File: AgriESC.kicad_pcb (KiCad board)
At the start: 2 copper layers, 94.5 x 53.5 mm, 309 parts, among them J1 SUPPLY, J10 GPIO, J11 USB_OTG, J12 HALL_ENC, J2 PH_A, J3 PH_B, J4 PH_C, J6 COMM, J7 SERVO, J8 CAN, J9 SWD, SW1 SW_SPDT, U1 FDMS7698, U10 STM32F405RGT6, U11 DRV8303, U12 TJA1051TK-3, U13 LMR16006YQ, U14 MCP1700-3302E_SOT23, U15 MCP1700-3302E_SOT23, U2 FDMS7698, U3 FDMS7698, U4 FDMS7698, U5 FDMS7698, U6 FDMS7698, U7 MAX9920, U8 MAX9920, U9 MAX9920, Y1 8M Resonator

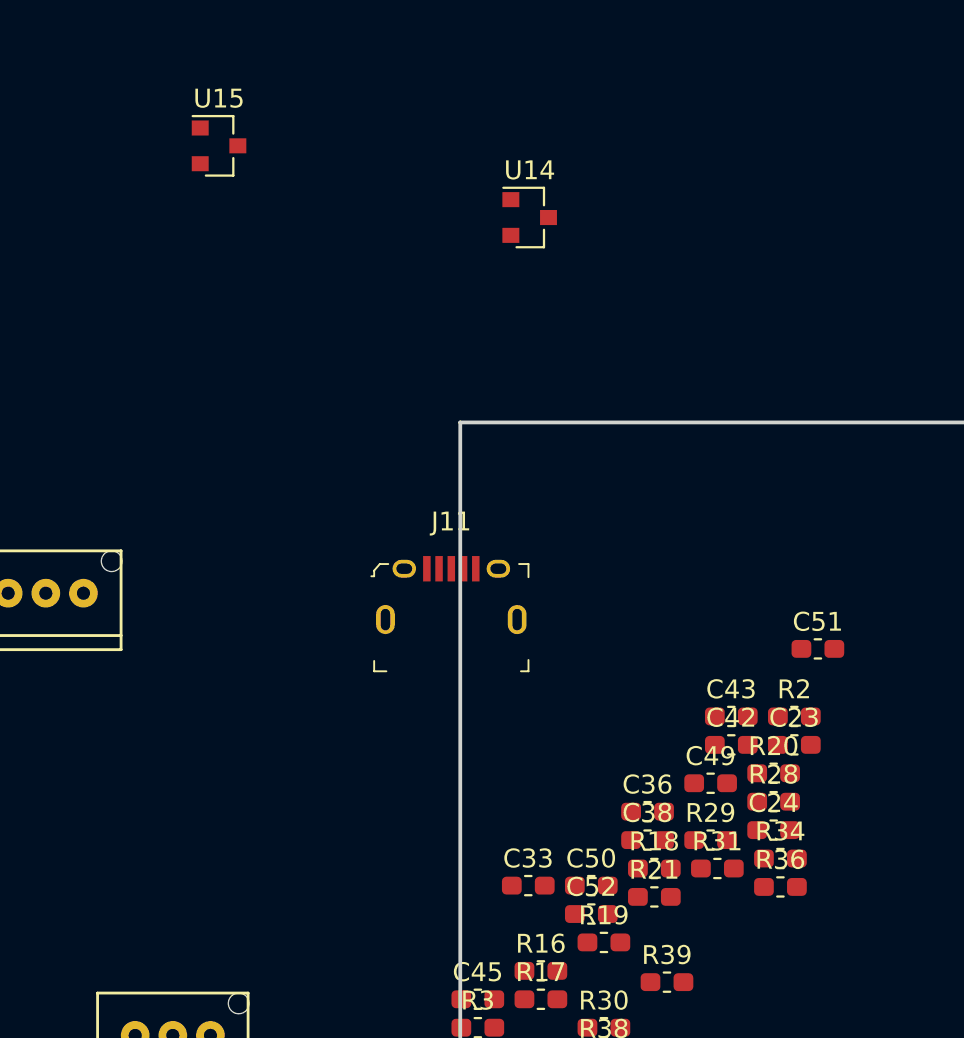
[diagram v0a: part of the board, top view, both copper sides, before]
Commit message: Wired up LDOs
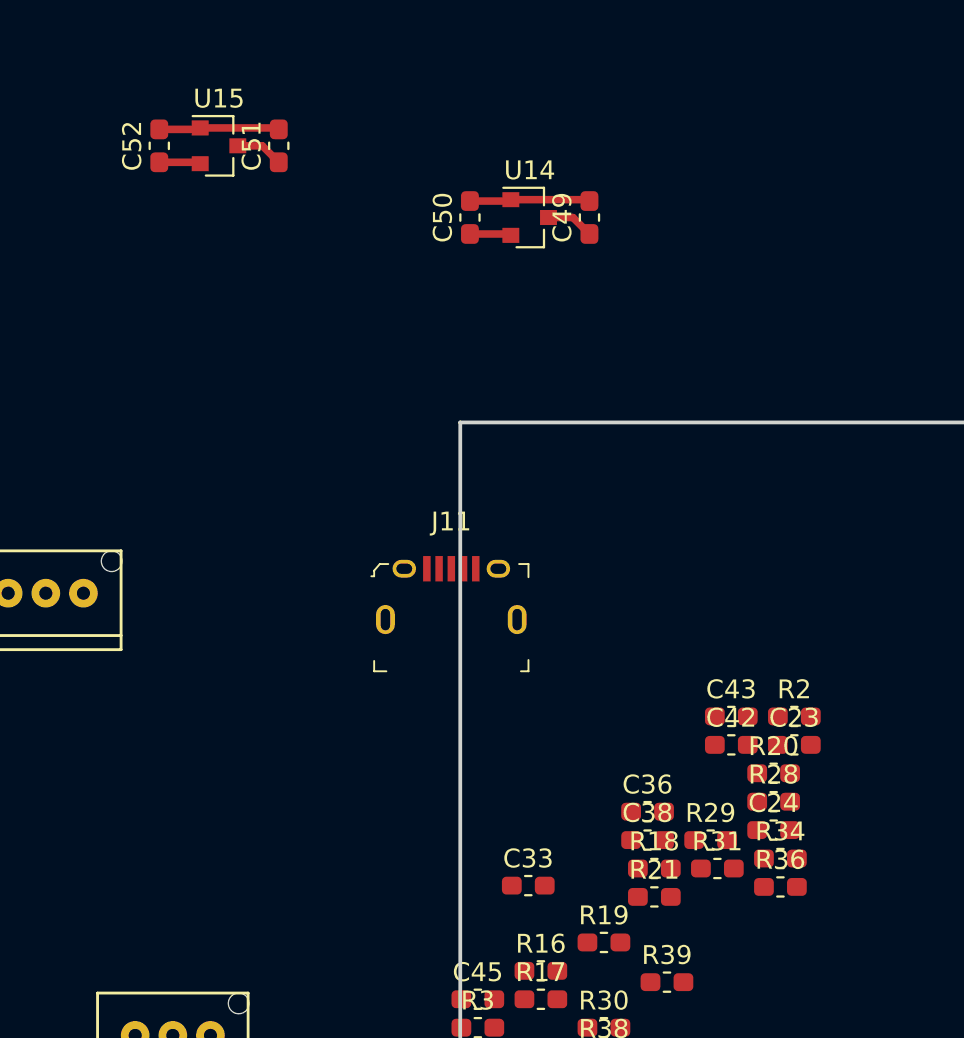
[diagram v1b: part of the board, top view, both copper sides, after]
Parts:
- moved C52 46.8 mm to (40.0, -12.7), turned to 90 degrees
- moved C51 39.2 mm to (46.4, -12.7), turned to 90 degrees
- moved C50 36.1 mm to (56.5, -8.89), turned to 90 degrees
- moved C49 30.7 mm to (62.9, -8.89), turned to 90 degrees
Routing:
- net SL_A: track 163.3 -> 176.1 mm
- net +5V: track 23.9 -> 29.0 mm
- net VCC: track 0.00 -> 2.21 mm
- net VAA: track 87.1 -> 89.3 mm
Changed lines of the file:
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@@
     (thickness 1.6)
     (drawings 4)
-    (tracks 336)
+    (tracks 352)
     (zones 0)
     (modules 309)
@@
   )
   (setup
-    (last_trace_width 0.2)
+    (last_trace_width 0.4)
     (user_trace_width 0.2)
     (user_trace_width 0.3)
@@
   )
   (module Capacitor_SMD:C_0603_1608Metric_Pad1.05x0.95mm_HandSolder (layer F.Cu)
-    (at 69.305001 21.175001)
+    (at 62.865 -8.89 90)
     (descr "Capacitor SMD 0603 (1608 Metric), square (rectangular) end terminal, IPC_7351 nominal with elongated pad for handsoldering. (Body size source: http://www.tortai-tech.com/upload/download/2011102023233369053.pdf), generated with kicad-footprint-generator")
     (tags "capacitor handsolder")
     (attr smd)
-    (fp_text reference C49 (at 0 -1.43) (layer F.SilkS)
+    (fp_text reference C49 (at 0 -1.43 90) (layer F.SilkS)
       (effects (font (size 1 1) (thickness 0.15)))
     )
-    (fp_text value 2u2_5V (at 0 1.43) (layer F.Fab)
+    (fp_text value 2u2_5V (at 0 1.43 90) (layer F.Fab)
       (effects (font (size 1 1) (thickness 0.15)))
     )
-    (fp_text user %R (at 0 0) (layer F.Fab)
+    (fp_text user %R (at 0 0 90) (layer F.Fab)
       (effects (font (size 0.4 0.4) (thickness 0.06)))
     )
@@
     (fp_line (start -0.8 -0.4) (end 0.8 -0.4) (layer F.Fab) (width 0.1))
     (fp_line (start -0.8 0.4) (end -0.8 -0.4) (layer F.Fab) (width 0.1))
-    (pad 2 smd roundrect (at 0.875 0) (size 1.05 0.95) (layers F.Cu F.Paste F.Mask) (roundrect_rratio 0.25)
+    (pad 2 smd roundrect (at 0.875 0 90) (size 1.05 0.95) (layers F.Cu F.Paste F.Mask) (roundrect_rratio 0.25)
       (net 1 SL_A))
-    (pad 1 smd roundrect (at -0.875 0) (size 1.05 0.95) (layers F.Cu F.Paste F.Mask) (roundrect_rratio 0.25)
+    (pad 1 smd roundrect (at -0.875 0 90) (size 1.05 0.95) (layers F.Cu F.Paste F.Mask) (roundrect_rratio 0.25)
       (net 23 +5V))
     (model ${KISYS3DMOD}/Capacitor_SMD.3dshapes/C_0603_1608Metric.wrl
@@
   )
   (module Capacitor_SMD:C_0603_1608Metric_Pad1.05x0.95mm_HandSolder (layer F.Cu)
-    (at 62.965001 26.615001)
+    (at 56.515 -8.89 90)
     (descr "Capacitor SMD 0603 (1608 Metric), square (rectangular) end terminal, IPC_7351 nominal with elongated pad for handsoldering. (Body size source: http://www.tortai-tech.com/upload/download/2011102023233369053.pdf), generated with kicad-footprint-generator")
     (tags "capacitor handsolder")
     (attr smd)
-    (fp_text reference C50 (at 0 -1.43) (layer F.SilkS)
+    (fp_text reference C50 (at 0 -1.43 90) (layer F.SilkS)
       (effects (font (size 1 1) (thickness 0.15)))
     )
-    (fp_text value 2u2_3V3 (at 0 1.43) (layer F.Fab)
+    (fp_text value 2u2_3V3 (at 0 1.43 90) (layer F.Fab)
       (effects (font (size 1 1) (thickness 0.15)))
     )
@@
     (fp_line (start 1.65 -0.73) (end 1.65 0.73) (layer F.CrtYd) (width 0.05))
     (fp_line (start 1.65 0.73) (end -1.65 0.73) (layer F.CrtYd) (width 0.05))
-    (fp_text user %R (at 0 0) (layer F.Fab)
+    (fp_text user %R (at 0 0 90) (layer F.Fab)
       (effects (font (size 0.4 0.4) (thickness 0.06)))
     )
-    (pad 1 smd roundrect (at -0.875 0) (size 1.05 0.95) (layers F.Cu F.Paste F.Mask) (roundrect_rratio 0.25)
+    (pad 1 smd roundrect (at -0.875 0 90) (size 1.05 0.95) (layers F.Cu F.Paste F.Mask) (roundrect_rratio 0.25)
       (net 4 VCC))
-    (pad 2 smd roundrect (at 0.875 0) (size 1.05 0.95) (layers F.Cu F.Paste F.Mask) (roundrect_rratio 0.25)
+    (pad 2 smd roundrect (at 0.875 0 90) (size 1.05 0.95) (layers F.Cu F.Paste F.Mask) (roundrect_rratio 0.25)
       (net 1 SL_A))
     (model ${KISYS3DMOD}/Capacitor_SMD.3dshapes/C_0603_1608Metric.wrl
@@
   )
   (module Capacitor_SMD:C_0603_1608Metric_Pad1.05x0.95mm_HandSolder (layer F.Cu)
-    (at 75.005001 14.035001)
+    (at 46.355 -12.7 90)
     (descr "Capacitor SMD 0603 (1608 Metric), square (rectangular) end terminal, IPC_7351 nominal with elongated pad for handsoldering. (Body size source: http://www.tortai-tech.com/upload/download/2011102023233369053.pdf), generated with kicad-footprint-generator")
     (tags "capacitor handsolder")
     (attr smd)
-    (fp_text reference C51 (at 0 -1.43) (layer F.SilkS)
+    (fp_text reference C51 (at 0 -1.43 90) (layer F.SilkS)
       (effects (font (size 1 1) (thickness 0.15)))
     )
-    (fp_text value 2u2_5V (at 0 1.43) (layer F.Fab)
+    (fp_text value 2u2_5V (at 0 1.43 90) (layer F.Fab)
       (effects (font (size 1 1) (thickness 0.15)))
     )
-    (fp_text user %R (at 0 0) (layer F.Fab)
+    (fp_text user %R (at 0 0 90) (layer F.Fab)
       (effects (font (size 0.4 0.4) (thickness 0.06)))
     )
@@
     (fp_line (start -0.8 -0.4) (end 0.8 -0.4) (layer F.Fab) (width 0.1))
     (fp_line (start -0.8 0.4) (end -0.8 -0.4) (layer F.Fab) (width 0.1))
-    (pad 2 smd roundrect (at 0.875 0) (size 1.05 0.95) (layers F.Cu F.Paste F.Mask) (roundrect_rratio 0.25)
+    (pad 2 smd roundrect (at 0.875 0 90) (size 1.05 0.95) (layers F.Cu F.Paste F.Mask) (roundrect_rratio 0.25)
       (net 1 SL_A))
-    (pad 1 smd roundrect (at -0.875 0) (size 1.05 0.95) (layers F.Cu F.Paste F.Mask) (roundrect_rratio 0.25)
+    (pad 1 smd roundrect (at -0.875 0 90) (size 1.05 0.95) (layers F.Cu F.Paste F.Mask) (roundrect_rratio 0.25)
       (net 23 +5V))
     (model ${KISYS3DMOD}/Capacitor_SMD.3dshapes/C_0603_1608Metric.wrl
@@
   )
   (module Capacitor_SMD:C_0603_1608Metric_Pad1.05x0.95mm_HandSolder (layer F.Cu)
-    (at 62.965001 28.125001)
+    (at 40.005 -12.7 90)
     (descr "Capacitor SMD 0603 (1608 Metric), square (rectangular) end terminal, IPC_7351 nominal with elongated pad for handsoldering. (Body size source: http://www.tortai-tech.com/upload/download/2011102023233369053.pdf), generated with kicad-footprint-generator")
     (tags "capacitor handsolder")
     (attr smd)
-    (fp_text reference C52 (at 0 -1.43) (layer F.SilkS)
+    (fp_text reference C52 (at 0 -1.43 90) (layer F.SilkS)
       (effects (font (size 1 1) (thickness 0.15)))
     )
-    (fp_text value 2u2_3V3 (at 0 1.43) (layer F.Fab)
+    (fp_text value 2u2_3V3 (at 0 1.43 90) (layer F.Fab)
       (effects (font (size 1 1) (thickness 0.15)))
     )
-    (fp_text user %R (at 0 0) (layer F.Fab)
+    (fp_text user %R (at 0 0 90) (layer F.Fab)
       (effects (font (size 0.4 0.4) (thickness 0.06)))
     )
@@
     (fp_line (start -0.8 -0.4) (end 0.8 -0.4) (layer F.Fab) (width 0.1))
     (fp_line (start -0.8 0.4) (end -0.8 -0.4) (layer F.Fab) (width 0.1))
-    (pad 2 smd roundrect (at 0.875 0) (size 1.05 0.95) (layers F.Cu F.Paste F.Mask) (roundrect_rratio 0.25)
+    (pad 2 smd roundrect (at 0.875 0 90) (size 1.05 0.95) (layers F.Cu F.Paste F.Mask) (roundrect_rratio 0.25)
       (net 1 SL_A))
-    (pad 1 smd roundrect (at -0.875 0) (size 1.05 0.95) (layers F.Cu F.Paste F.Mask) (roundrect_rratio 0.25)
+    (pad 1 smd roundrect (at -0.875 0 90) (size 1.05 0.95) (layers F.Cu F.Paste F.Mask) (roundrect_rratio 0.25)
       (net 3 VAA))
     (model ${KISYS3DMOD}/Capacitor_SMD.3dshapes/C_0603_1608Metric.wrl
@@
   (segment (start 59.055 93.345) (end 59.055 93.98) (width 0.4) (layer F.Cu) (net 1))
   (segment (start 59.69 94.615) (end 59.055 93.98) (width 0.4) (layer F.Cu) (net 1))
+  (segment (start 42.105 -13.575) (end 42.18 -13.65) (width 0.4) (layer F.Cu) (net 1))
+  (segment (start 40.005 -13.575) (end 42.105 -13.575) (width 0.4) (layer F.Cu) (net 1))
+  (segment (start 46.28 -13.65) (end 46.355 -13.575) (width 0.4) (layer F.Cu) (net 1))
+  (segment (start 42.18 -13.65) (end 46.28 -13.65) (width 0.4) (layer F.Cu) (net 1))
+  (segment (start 58.615 -9.765) (end 58.69 -9.84) (width 0.4) (layer F.Cu) (net 1))
+  (segment (start 56.515 -9.765) (end 58.615 -9.765) (width 0.4) (layer F.Cu) (net 1))
+  (segment (start 62.79 -9.84) (end 62.865 -9.765) (width 0.4) (layer F.Cu) (net 1))
+  (segment (start 58.69 -9.84) (end 62.79 -9.84) (width 0.4) (layer F.Cu) (net 1))
   (segment (start 114.775 22.975) (end 114.75 23) (width 0.25) (layer F.Cu) (net 2))
   (segment (start 114.775 21) (end 114.775 22.975) (width 0.25) (layer F.Cu) (net 2))
@@
   (segment (start 130 54.75) (end 129.75 54.75) (width 0.4) (layer B.Cu) (net 3))
   (segment (start 129.75 54.75) (end 117.75 54.75) (width 0.4) (layer B.Cu) (net 3))
+  (segment (start 42.105 -11.825) (end 42.18 -11.75) (width 0.4) (layer F.Cu) (net 3))
+  (segment (start 40.005 -11.825) (end 42.105 -11.825) (width 0.4) (layer F.Cu) (net 3))
+  (segment (start 58.615 -8.015) (end 58.69 -7.94) (width 0.4) (layer F.Cu) (net 4))
+  (segment (start 56.515 -8.015) (end 58.615 -8.015) (width 0.4) (layer F.Cu) (net 4))
   (segment (start 119.217 34.5) (end 119.25 34.5) (width 0.2) (layer F.Cu) (net 12))
   (segment (start 117.405 36.312) (end 119.217 34.5) (width 0.2) (layer F.Cu) (net 12))
@@
   (segment (start 50.56 86.935) (end 49.73499 87.76001) (width 0.2) (layer F.Cu) (net 23))
   (segment (start 50.56 86.36) (end 50.56 86.935) (width 0.2) (layer F.Cu) (net 23))
+  (segment (start 45.48 -12.7) (end 46.355 -11.825) (width 0.4) (layer F.Cu) (net 23))
+  (segment (start 44.18 -12.7) (end 45.48 -12.7) (width 0.4) (layer F.Cu) (net 23))
+  (segment (start 61.99 -8.89) (end 62.865 -8.015) (width 0.4) (layer F.Cu) (net 23))
+  (segment (start 60.69 -8.89) (end 61.99 -8.89) (width 0.4) (layer F.Cu) (net 23))
   (segment (start 58.07 88.73) (end 59.17 87.63) (width 0.4) (layer F.Cu) (net 25))
   (segment (start 56.195 88.73) (end 58.07 88.73) (width 0.4) (layer F.Cu) (net 25))

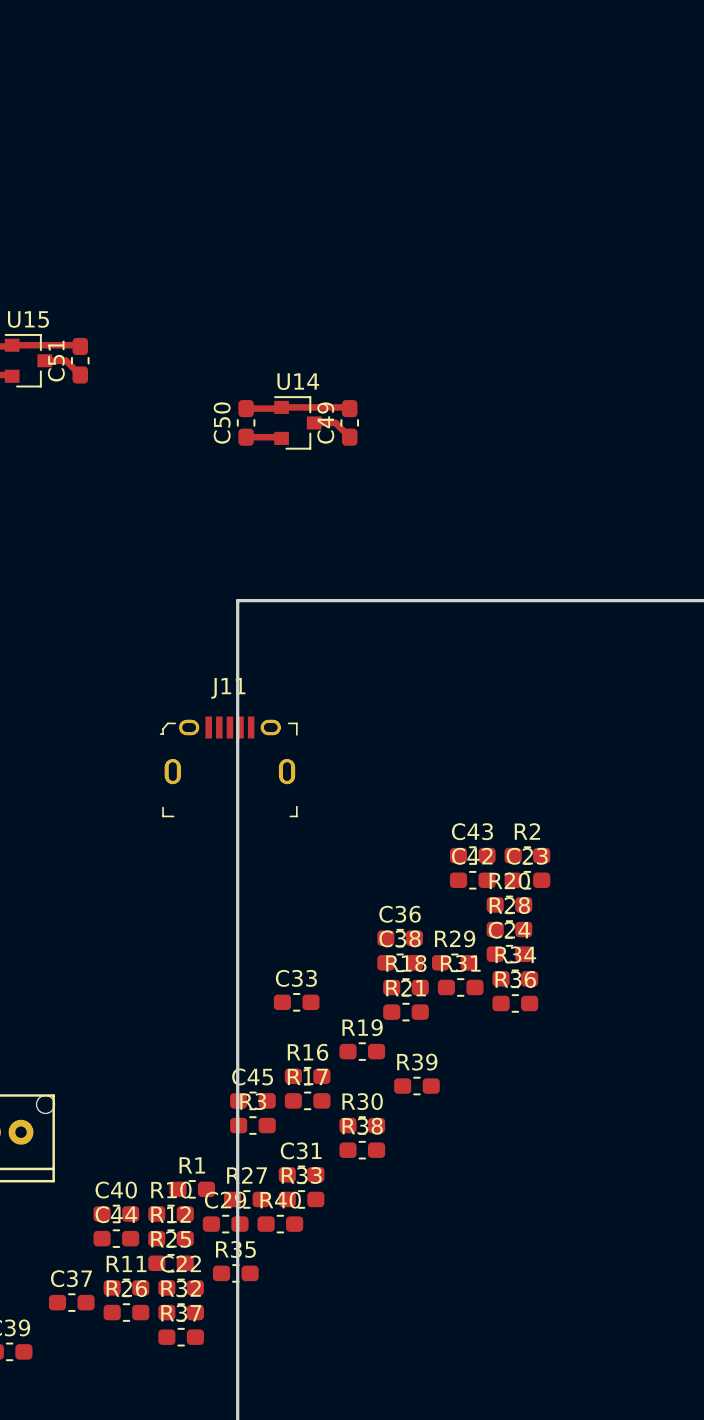
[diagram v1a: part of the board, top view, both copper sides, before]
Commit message: Added USB wiring
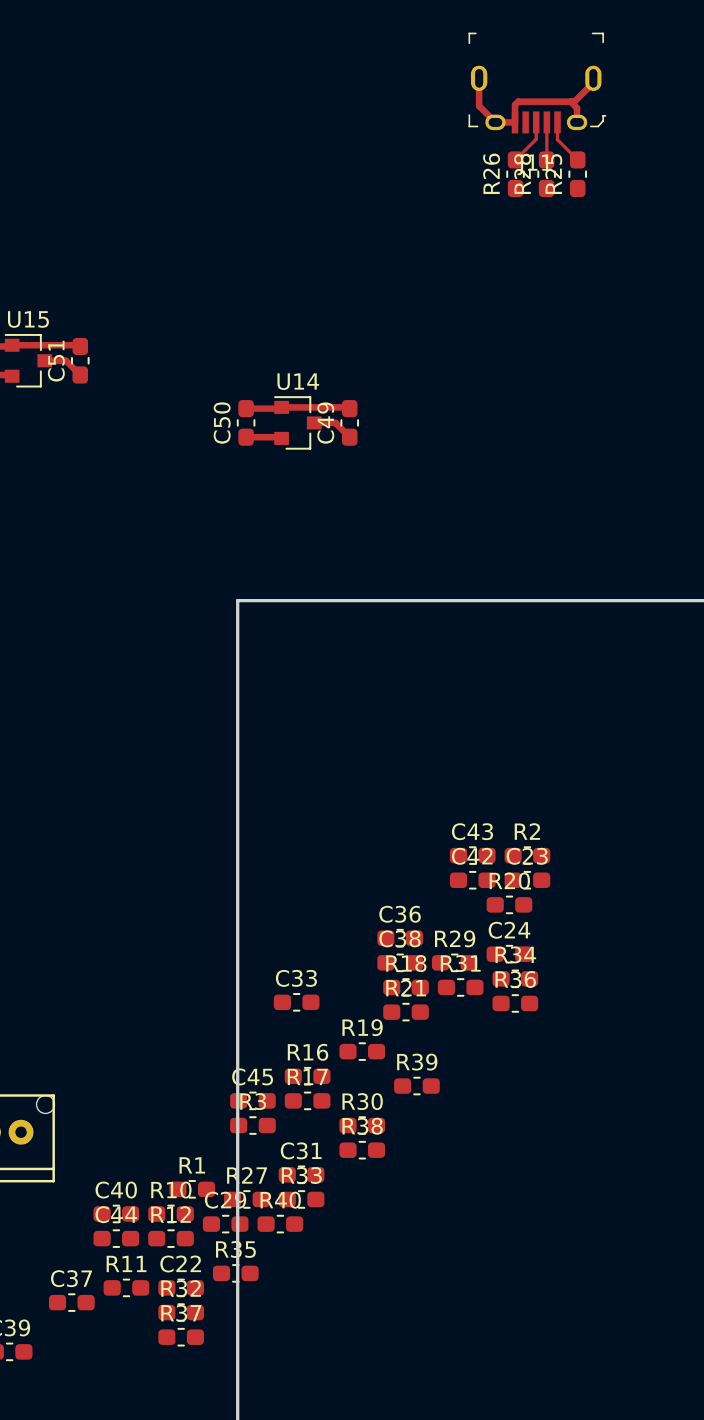
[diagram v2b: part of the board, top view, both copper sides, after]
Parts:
- moved R26 73.7 mm to (73.0, -24.1), turned to 90 degrees
- moved R25 71.2 mm to (76.8, -24.1), turned to 90 degrees
- moved R28 46.3 mm to (74.9, -24.1), turned to 90 degrees
- moved J11 41.6 mm to (74.3, -27.3), turned to 180 degrees
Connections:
- J11 pad SH: (no net) -> SL_A
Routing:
- net SL_A: track 176.1 -> 188.6 mm
- net Net-(J11-Pad3): track 0.00 -> 2.83 mm
- net Net-(J11-Pad1): track 0.00 -> 2.81 mm
- net Net-(J11-Pad2): track 0.00 -> 2.31 mm

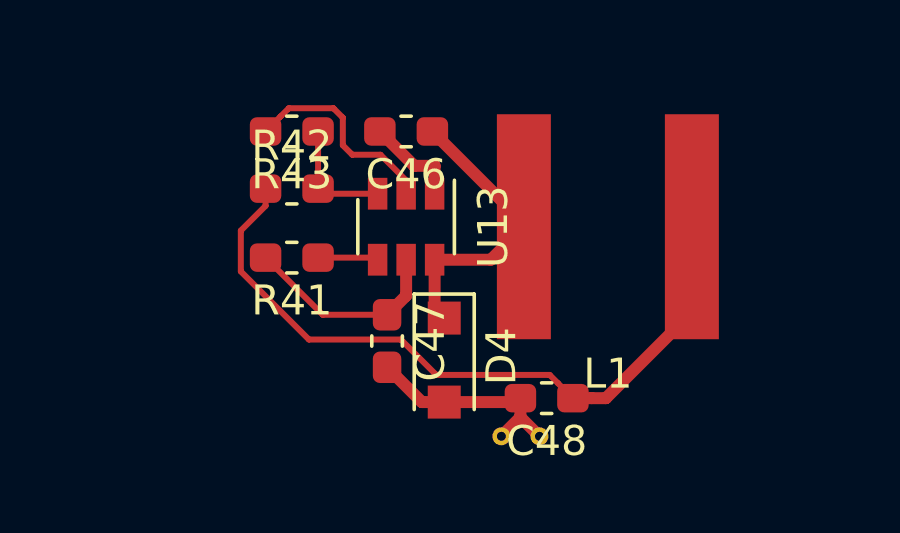
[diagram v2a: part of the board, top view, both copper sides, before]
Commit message: Finished USB ground
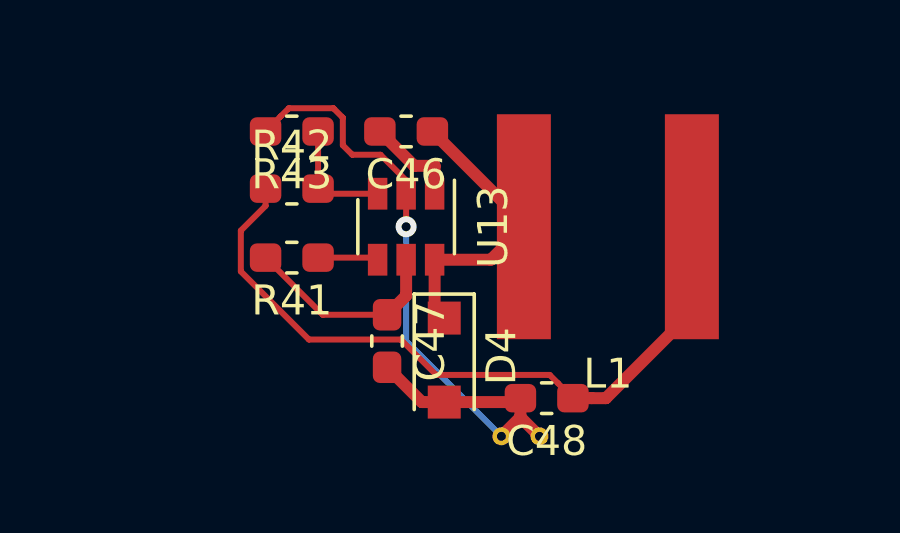
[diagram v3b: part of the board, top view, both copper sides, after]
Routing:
- net SL_A: track 188.6 -> 198.0 mm, vias 9 -> 10
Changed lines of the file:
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@@
     (thickness 1.6)
     (drawings 4)
-    (tracks 369)
+    (tracks 373)
     (zones 0)
     (modules 309)
@@
   (segment (start 76.64 -28.575) (end 77.795 -29.73) (width 0.4) (layer F.Cu) (net 1))
   (segment (start 76.4 -28.575) (end 76.64 -28.575) (width 0.4) (layer F.Cu) (net 1))
+  (via (at 55.245 87.63) (size 0.7) (drill 0.3) (layers F.Cu B.Cu) (net 1))
+  (segment (start 55.245 86.53) (end 55.245 87.63) (width 0.2) (layer F.Cu) (net 1))
+  (segment (start 55.245 91.44) (end 58.42 94.615) (width 0.2) (layer B.Cu) (net 1))
+  (segment (start 55.245 87.63) (end 55.245 91.44) (width 0.2) (layer B.Cu) (net 1))
   (segment (start 114.775 22.975) (end 114.75 23) (width 0.25) (layer F.Cu) (net 2))
   (segment (start 114.775 21) (end 114.775 22.975) (width 0.25) (layer F.Cu) (net 2))
